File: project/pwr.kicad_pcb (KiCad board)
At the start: 2 copper layers, 77.5 x 75 mm, 134 parts, among them J101 IDC 2x8, J201 XT-IN, J202 METER, J203 XT-OUT, J301 XT-IN, J302 METER, J303 XT-OUT, J401 XT-IN, J402 METER, J403 XT-OUT, J501 XT-IN, J502 METER, J503 XT-OUT, J601 XT-IN, J602 METER, J603 XT-OUT, Q201 AON6144, Q301 AON6144, Q401 AON6144, Q501 AON6144, Q601 AON6144, U101 USBLC6-2SC6, U102 USBLC6-2SC6, U103 USBLC6-2SC6, U104 USBLC6-2SC6, U105 TMP102AIDRLR, U106 TMP102AIDRLR, U201 UCC27517DBVR, U301 UCC27517DBVR, U401 UCC27517DBVR, U501 UCC27517DBVR, U601 UCC27517DBVR

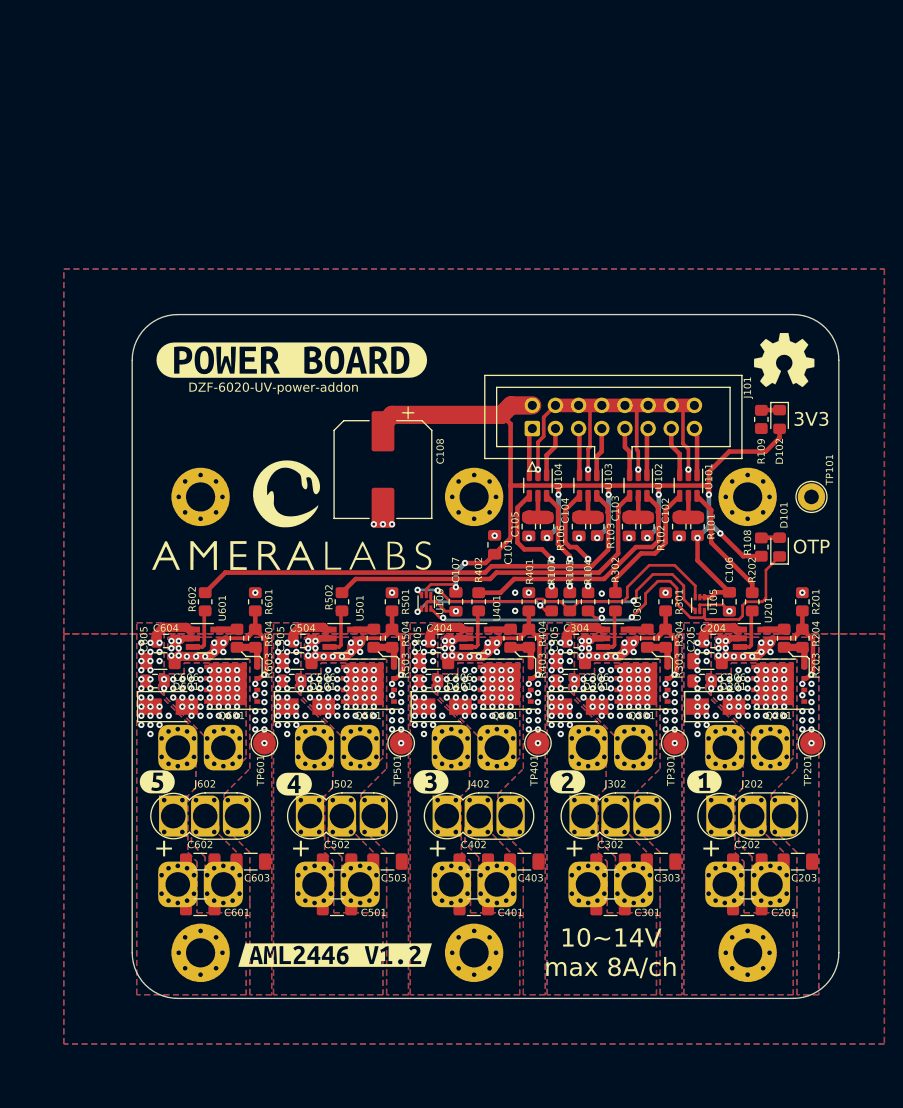
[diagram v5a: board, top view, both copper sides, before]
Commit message: using isolated gate driver
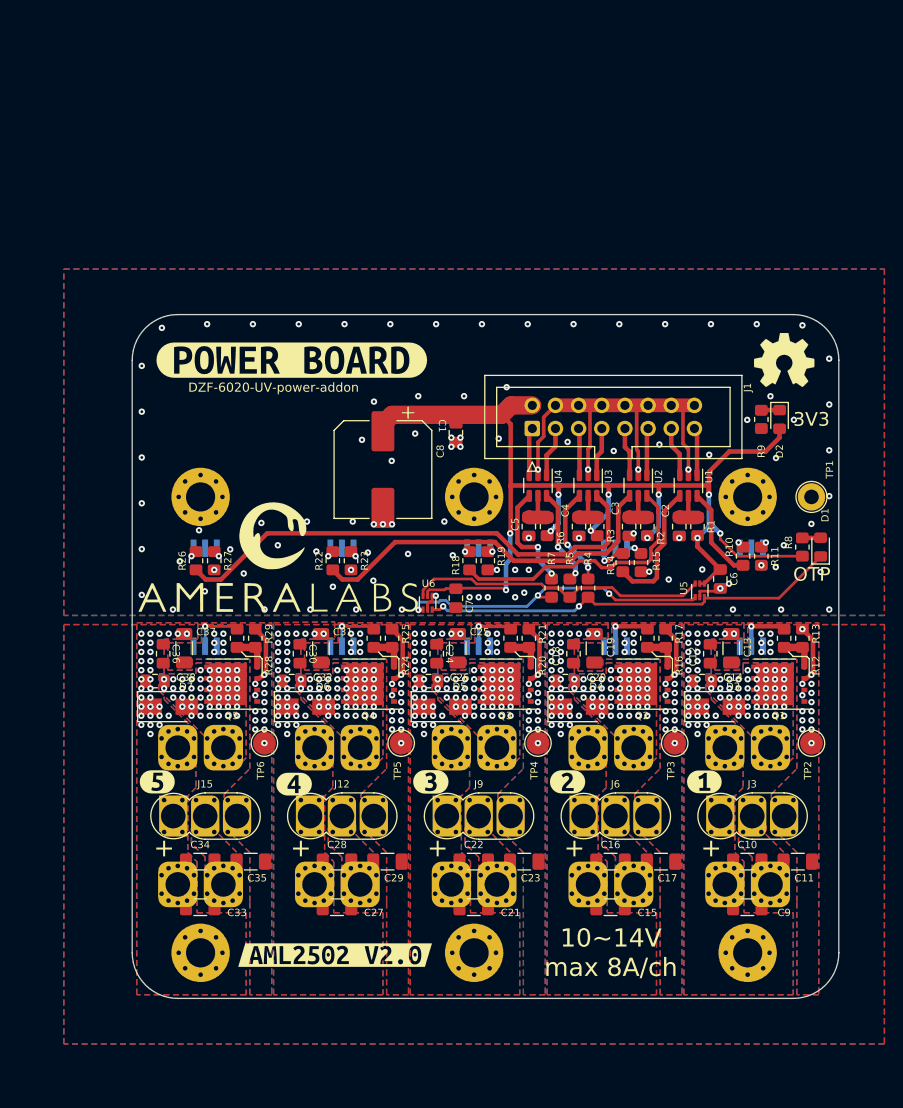
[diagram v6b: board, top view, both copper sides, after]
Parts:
- removed R201, R301, R401, R501, R601: 10R, Resistor_SMD:R_0805_2012Metric_Pad1.20x1.40mm_HandSolder
- removed R202, R302, R402, R502, R602: 100R, Resistor_SMD:R_0805_2012Metric_Pad1.20x1.40mm_HandSolder
- removed U201, U301, U401, U501, U601: UCC27517DBVR, Package_TO_SOT_SMD:SOT-23-5_HandSoldering
- removed kibuzzard-6736C30A: G***, kibuzzard-6736C30A
- added R10: 68R, Resistor_SMD:R_0805_2012Metric_Pad1.20x1.40mm_HandSolder, F.Cu at (178.5, 81.5)
- added R11: 68R, Resistor_SMD:R_0805_2012Metric_Pad1.20x1.40mm_HandSolder, F.Cu at (180.5, 81.5)
- added R14: 68R, Resistor_SMD:R_0805_2012Metric_Pad1.20x1.40mm_HandSolder, F.Cu at (165.3, 82.2)
- added R15: 68R, Resistor_SMD:R_0805_2012Metric_Pad1.20x1.40mm_HandSolder, F.Cu at (167.3, 82.2)
- added R18: 68R, Resistor_SMD:R_0805_2012Metric_Pad1.20x1.40mm_HandSolder, F.Cu at (148.5, 82.0)
- added R19: 68R, Resistor_SMD:R_0805_2012Metric_Pad1.20x1.40mm_HandSolder, F.Cu at (150.5, 82.0)
- added R22: 68R, Resistor_SMD:R_0805_2012Metric_Pad1.20x1.40mm_HandSolder, F.Cu at (133.5, 82.0)
- added R23: 68R, Resistor_SMD:R_0805_2012Metric_Pad1.20x1.40mm_HandSolder, F.Cu at (135.5, 82.0)
- added R26: 68R, Resistor_SMD:R_0805_2012Metric_Pad1.20x1.40mm_HandSolder, F.Cu at (118.5, 82.0)
- added R27: 68R, Resistor_SMD:R_0805_2012Metric_Pad1.20x1.40mm_HandSolder, F.Cu at (120.5, 82.0)
- added U10: SLM346CK-DG, Package_SO:SSO-6_6.8x4.6mm_P1.27mm_Clearance8mm, B.Cu at (134.5, 86.0)
- added U11: SLM346CK-DG, Package_SO:SSO-6_6.8x4.6mm_P1.27mm_Clearance8mm, B.Cu at (119.5, 86.0)
- added U7: SLM346CK-DG, Package_SO:SSO-6_6.8x4.6mm_P1.27mm_Clearance8mm, B.Cu at (179.4, 86.0)
- added U8: SLM346CK-DG, Package_SO:SSO-6_6.8x4.6mm_P1.27mm_Clearance8mm, B.Cu at (164.5, 86.0)
- added U9: SLM346CK-DG, Package_SO:SSO-6_6.8x4.6mm_P1.27mm_Clearance8mm, B.Cu at (149.5, 86.0)
- added kibuzzard-6780C605: G***, kibuzzard-6780C605, F.Cu at (133.8, 125.2)
- moved kibuzzard-66D17D14 47.9 mm to (131.0, 75.5)
- moved C1 13.0 mm to (147.0, 68.0), turned to 90 degrees
- moved G1 4.84 mm to (127.5, 81.6)
- moved D1 4.50 mm to (187.0, 80.5)
- moved R8 4.50 mm to (185.0, 80.5)
- moved C37 2.95 mm to (117.2, 91.6), turned to -90 degrees
- moved C13 2.95 mm to (177.2, 91.6), turned to -90 degrees
- moved C19 2.95 mm to (162.2, 91.6), turned to -90 degrees
- moved C25 2.95 mm to (147.2, 91.6), turned to -90 degrees
- moved C31 2.95 mm to (132.2, 91.6), turned to -90 degrees
- moved C6 2.69 mm to (176.0, 84.0)
- moved kibuzzard-6705D925 2.00 mm to (119.5, 96.0)
- moved kibuzzard-6705D93C 2.00 mm to (134.5, 96.0)
- moved kibuzzard-6705D966 2.00 mm to (149.5, 96.0)
- moved kibuzzard-6705D971 2.00 mm to (164.5, 96.0)
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- renumbered C101 to C1, C202 to C10, C203 to C11, C204 to C12, C205 to C13, C206 to C14, C301 to C15, C302 to C16, C303 to C17, C304 to C18, C305 to C19, C102 to C2, C306 to C20, C401 to C21, C402 to C22, C403 to C23, C404 to C24, C405 to C25, C406 to C26, C501 to C27, C502 to C28, C503 to C29, C103 to C3, C504 to C30, C505 to C31, C506 to C32, C601 to C33, C602 to C34, C603 to C35, C604 to C36, C605 to C37, C606 to C38, C104 to C4, C105 to C5, C106 to C6, C107 to C7, C108 to C8, C201 to C9, D101 to D1, D102 to D2, D201 to D3, D301 to D4, D401 to D5, D501 to D6, D601 to D7, G101 to G1, G102 to G2, H101 to H1, H102 to H2, H103 to H3, H104 to H4, H105 to H5, H106 to H6, J101 to J1, J403 to J10, J501 to J11, J502 to J12, J503 to J13, J601 to J14, J602 to J15, J603 to J16, J201 to J2, J202 to J3, J203 to J4, J301 to J5, J302 to J6, J303 to J7, J401 to J8, J402 to J9, Q201 to Q1, Q301 to Q2, Q401 to Q3, Q501 to Q4, Q601 to Q5, R101 to R1, R203 to R12, R204 to R13, R303 to R16, R304 to R17, R102 to R2, R403 to R20, R404 to R21, R503 to R24, R504 to R25, R603 to R28, R604 to R29, R103 to R3, R104 to R4, R105 to R5, R106 to R6, R107 to R7, R108 to R8, R109 to R9, TP101 to TP1, TP201 to TP2, TP301 to TP3, TP401 to TP4, TP501 to TP5, TP601 to TP6, U101 to U1, U102 to U2, U103 to U3, U104 to U4, U105 to U5, U106 to U6
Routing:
- net /pwr_ch4/PGND: track 24.3 -> 6.43 mm, vias 26 -> 19
- net /pwr_ch3/PGND: track 24.3 -> 6.43 mm, vias 26 -> 19
- net /pwr_ch1/PGND: track 24.3 -> 6.43 mm, vias 26 -> 20
- net /pwr_ch5/PGND: track 24.3 -> 6.43 mm, vias 26 -> 19
- net /pwr_ch2/PGND: track 24.3 -> 6.43 mm, vias 26 -> 19
- net /ALERT_P: track 53.0 -> 46.4 mm, vias 3 -> 2
- net Net-(R602-Pad2): track 5.25 -> 0.00 mm
- net Net-(R302-Pad2): track 5.25 -> 0.00 mm
- net Net-(R202-Pad2): track 5.25 -> 0.00 mm
- net Net-(R502-Pad2): track 5.25 -> 0.00 mm
- net Net-(R402-Pad2): track 5.25 -> 0.00 mm
- net /pwr_ch3/Vcc: track 4.40 -> 0.00 mm, vias 28 -> 31
- net /pwr_ch2/Vcc: track 4.40 -> 0.00 mm, vias 28 -> 31
- net /pwr_ch5/Vcc: track 4.40 -> 0.00 mm, vias 28 -> 31
- net /pwr_ch4/Vcc: track 4.40 -> 0.00 mm, vias 28 -> 31
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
